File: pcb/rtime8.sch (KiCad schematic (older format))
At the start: 16 parts, among them J2 ICSP, J4 TEST, U5 PIC24FJ32GA004-I/PT, Y1 32768

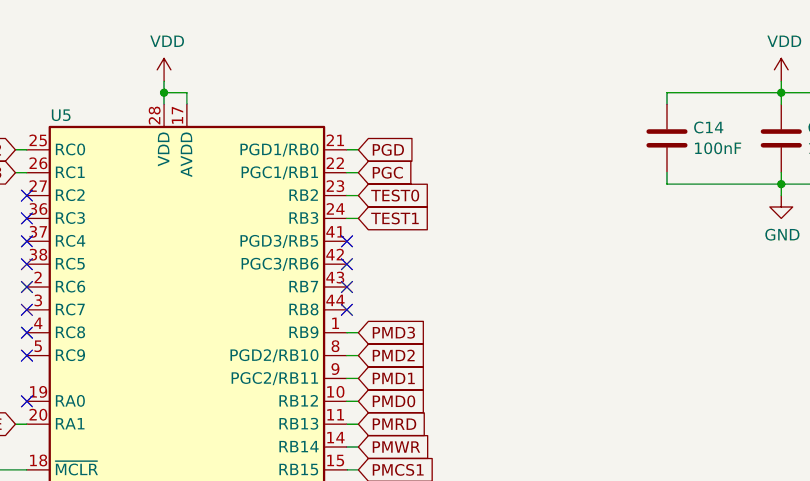
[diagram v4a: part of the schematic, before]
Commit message: PCB: Add connection for detecting power loss
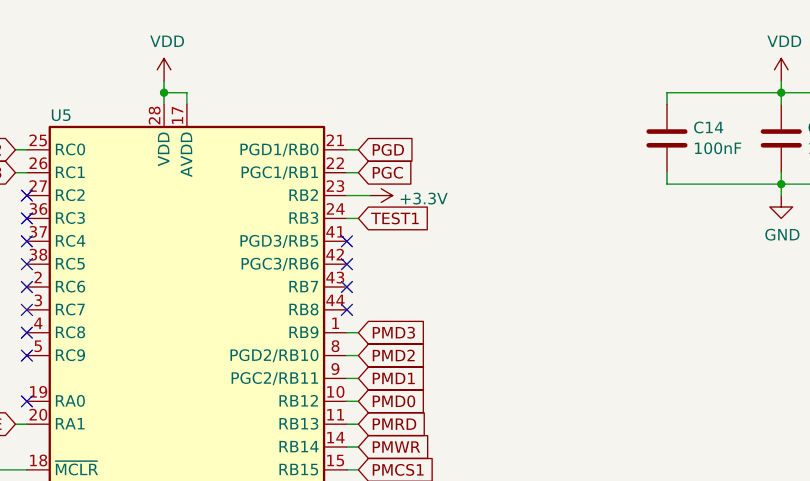
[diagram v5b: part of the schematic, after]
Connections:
- net +3V3: now also U5.23 (RB2)
- net TEST0: no longer U5.23 (RB2)
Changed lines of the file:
@@
 Wire Wire Line
 	2800 5250 2900 5250
-Text GLabel 6800 3000 2    50   Input ~ 0
-TEST0
 Text GLabel 6800 3100 2    50   Input ~ 0
 TEST1
@@
 	5350 2900 5300 2900
 Wire Wire Line
-	6800 3000 6750 3000
-Wire Wire Line
 	6750 3100 6800 3100
 Text Notes 8250 5000 2    50   ~ 0
@@
 Wire Wire Line
 	5300 4000 5350 4000
+$Comp
+L power:+3.3V #PWR0121
+U 1 1 6114F803
+P 6850 3000
+F 0 "#PWR0121" H 6850 2850 50  0001 C CNN
+F 1 "+3.3V" V 6865 3128 50  0000 L CNN
+F 2 "" H 6850 3000 50  0001 C CNN
+F 3 "" H 6850 3000 50  0001 C CNN
+	1    6850 3000
+	0    1    1    0
+$EndComp
+Wire Wire Line
+	6850 3000 6750 3000
 $EndSCHEMATC

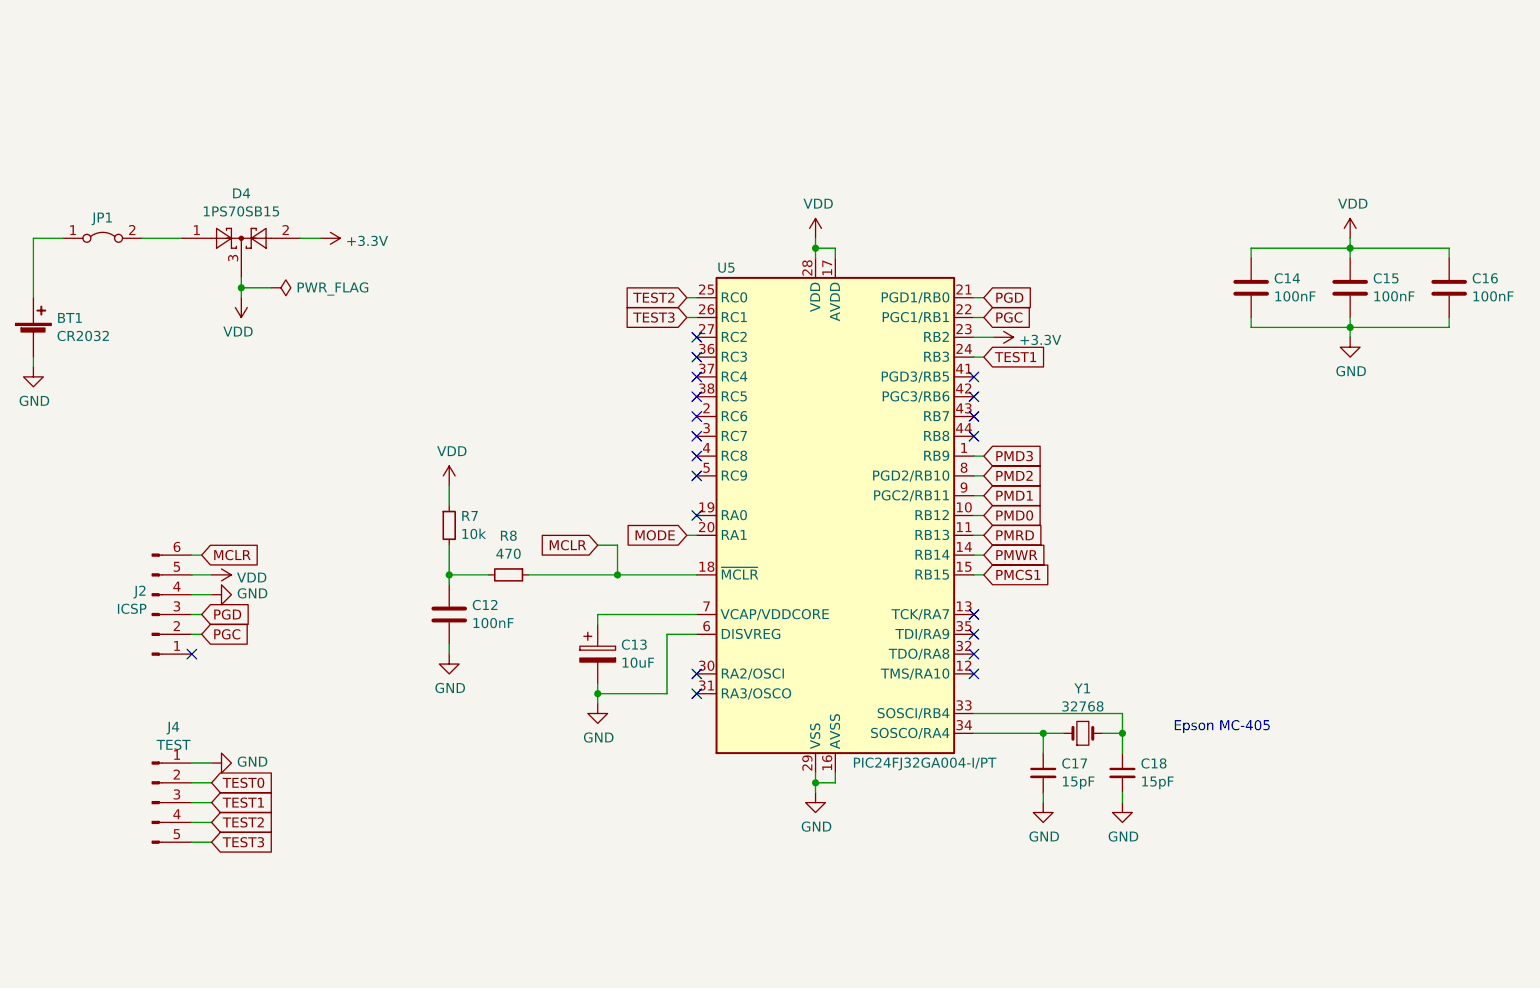
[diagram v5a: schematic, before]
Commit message: Switch to PIC24FJ64GB004 as RTime8 emulator
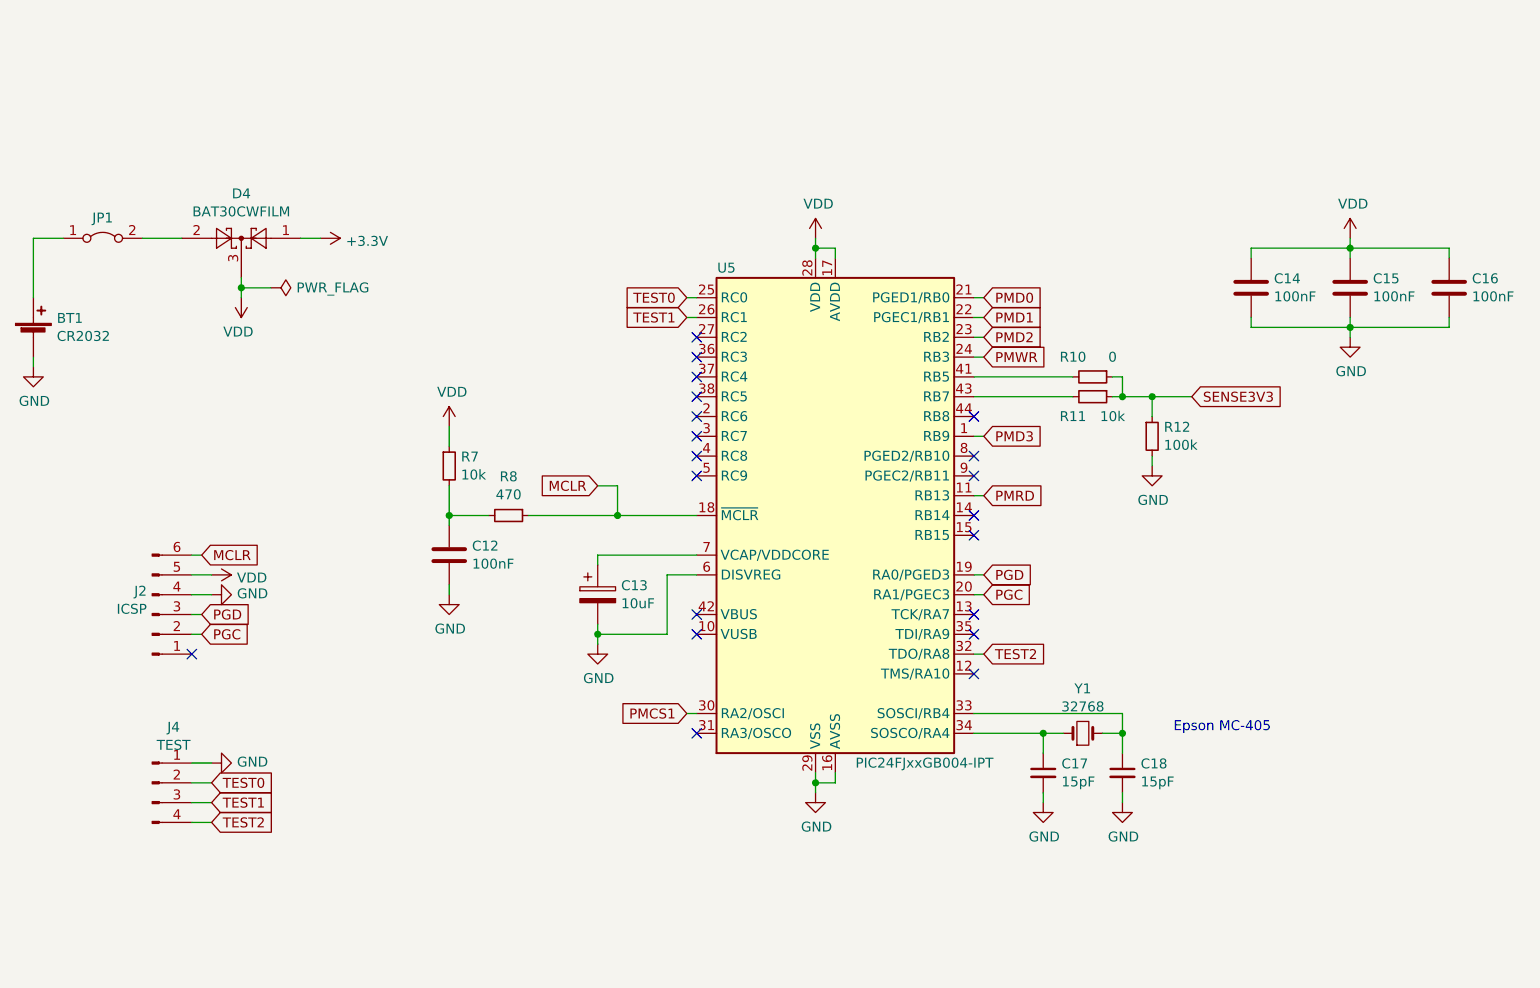
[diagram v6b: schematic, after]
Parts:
- removed J4: TEST, Connector_PinHeader_2.54mm:PinHeader_1x05_P2.54mm_Vertical, symbol Connector:Conn_01x05_Male
- removed U5: PIC24FJ32GA004-I/PT, Package_QFP:TQFP-44_10x10mm_P0.8mm, symbol My_Symbols:PIC24FJxxGA004-IPT
- added J4: TEST, Connector_PinHeader_2.54mm:PinHeader_1x04_P2.54mm_Vertical, symbol Connector:Conn_01x04_Male
- added R10: 0, Resistor_SMD:R_0805_2012Metric_Pad1.20x1.40mm_HandSolder, symbol Device:R_Small
- added R11: 10k, Resistor_SMD:R_0805_2012Metric_Pad1.20x1.40mm_HandSolder, symbol Device:R_Small
- added R12: 100k, Resistor_SMD:R_0805_2012Metric_Pad1.20x1.40mm_HandSolder, symbol Device:R_Small
- added U5: PIC24FJxxGB004-IPT, Package_QFP:TQFP-44_10x10mm_P0.8mm, symbol My_Symbols:PIC24FJxxGB004-IPT
- D4: value 1PS70SB15 -> BAT30CWFILM
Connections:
- net +3V3: now also D4.1; no longer D4.2
- net GND: now also J4.1 (Pin_1), R12.2, U5.16 (AVSS), U5.29 (VSS), U5.39 (VSS), U5.6 (DISVREG)
- net MCLR: now also U5.18 (~MCLR~)
- net PGC: now also U5.20 (RA1/PGEC3)
- net PGD: now also U5.19 (RA0/PGED3)
- net PMCS1: now also U5.30 (RA2/OSCI)
- net PMD0: now also U5.21 (PGED1/RB0)
- net PMD1: now also U5.22 (PGEC1/RB1)
- net PMD2: now also U5.23 (RB2)
- net PMD3: now also U5.1 (RB9)
- net PMRD: now also U5.11 (RB13)
- net PMWR: now also U5.24 (RB3)
- net TEST0: now also J4.2 (Pin_2), U5.25 (RC0)
- net TEST1: now also J4.3 (Pin_3), U5.26 (RC1)
- net TEST2: now also J4.4 (Pin_4), U5.32 (TDO/RA8)
- net VDD: now also U5.17 (AVDD), U5.28 (VDD), U5.40 (VDD)
- net at C18.1, Y1.2, Y1.3: now also U5.33 (SOSCI/RB4)
- net at C17.1, Y1.1, Y1.4: now also U5.34 (SOSCO/RA4)
- net at C13.1: now also U5.7 (VCAP/VDDCORE)
- net at JP1.2 (B): now also D4.2; no longer D4.1
- new net: R10.2, U5.41 (RB5)
- new net: R11.2, U5.43 (RB7)
- new net SENSE3V3: R10.1, R11.1, R12.1
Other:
- moved on the sheet: C12, C13, R7, R8
